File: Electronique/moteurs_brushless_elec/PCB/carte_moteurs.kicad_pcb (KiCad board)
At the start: 2 copper layers, 90 x 65 mm, 82 parts, among them J1 CONN_SERIAL, J2 swdio, J3 FAN, K1 Maxon-200142, K2 Maxon-200142, P1 CONN_I2C, P2 CONN_FREE, P3 CONN_CAN, P4 encoder_2, P5 encoder_1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

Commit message: Noms connecteurs brushless
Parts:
- Encodeur 1: renamed from P5
- Encodeur 2: renamed from P4
- renumbered P3 to CAN, P1 to I2C, P2 to Libre, J1 to Serial
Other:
- board text added: "FAN"
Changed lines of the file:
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@@
   (general
     (links 197)
-    (no_connects 6)
+    (no_connects 0)
     (area 51.6115 80.215 149.459001 152.8396)
     (thickness 1.6)
-    (drawings 14)
+    (drawings 15)
     (tracks 994)
     (zones 0)
@@
   )
   (setup
-    (last_trace_width 0.5)
+    (last_trace_width 1.2)
     (user_trace_width 0.25)
     (user_trace_width 0.5)
@@
     (descr "Connector Headers with Friction Lock, 22-27-2041, http://www.molex.com/pdm_docs/sd/022272021_sd.pdf")
     (tags "connector molex kk_6410 22-27-2041")
-    (fp_text reference P5 (at 1 -4.5) (layer F.SilkS)
+    (fp_text reference "Encodeur 1" (at 3.81 -4.572) (layer F.SilkS)
       (effects (font (size 1 1) (thickness 0.15)))
     )
@@
     (descr "Connector Headers with Friction Lock, 22-27-2021, http://www.molex.com/pdm_docs/sd/022272021_sd.pdf")
     (tags "connector molex kk_6410 22-27-2021")
-    (fp_text reference J1 (at 1 -4.5) (layer F.SilkS)
+    (fp_text reference Serial (at 1 -4.5) (layer F.SilkS)
       (effects (font (size 1 1) (thickness 0.15)))
     )
@@
     (descr "Connector Headers with Friction Lock, 22-27-2021, http://www.molex.com/pdm_docs/sd/022272021_sd.pdf")
     (tags "connector molex kk_6410 22-27-2021")
-    (fp_text reference P1 (at 1 -4.5) (layer F.SilkS)
+    (fp_text reference I2C (at 1.27 -4.572) (layer F.SilkS)
       (effects (font (size 1 1) (thickness 0.15)))
     )
@@
     (descr "Connector Headers with Friction Lock, 22-27-2021, http://www.molex.com/pdm_docs/sd/022272021_sd.pdf")
     (tags "connector molex kk_6410 22-27-2021")
-    (fp_text reference P2 (at 1 -4.5 270) (layer F.SilkS)
+    (fp_text reference Libre (at 1.016 4.826 270) (layer F.SilkS)
       (effects (font (size 1 1) (thickness 0.15)))
     )
@@
     (descr "Connector Headers with Friction Lock, 22-27-2021, http://www.molex.com/pdm_docs/sd/022272021_sd.pdf")
     (tags "connector molex kk_6410 22-27-2021")
-    (fp_text reference P3 (at 1 -4.5) (layer F.SilkS)
+    (fp_text reference CAN (at 1 -4.5) (layer F.SilkS)
       (effects (font (size 1 1) (thickness 0.15)))
     )
@@
     (descr "Connector Headers with Friction Lock, 22-27-2041, http://www.molex.com/pdm_docs/sd/022272021_sd.pdf")
     (tags "connector molex kk_6410 22-27-2041")
-    (fp_text reference P4 (at 1 -4.5 270) (layer F.SilkS)
+    (fp_text reference "Encodeur 2" (at 4.064 4.4704 270) (layer F.SilkS)
       (effects (font (size 1 1) (thickness 0.15)))
     )
@@
     (tags "SOIC 1.27")
     (attr smd)
-    (fp_text reference U9 (at 0 -3.5 180) (layer F.SilkS)
+    (fp_text reference U9 (at 4.826 0.254 180) (layer F.SilkS)
       (effects (font (size 1 1) (thickness 0.15)))
     )
@@
     )
   )
+  (gr_text FAN (at 65.532 146.304 90) (layer F.SilkS)
+    (effects (font (size 1.5 1.5) (thickness 0.3)))
+  )
   (gr_text +3.3V (at 92.8624 91.8464) (layer F.SilkS)

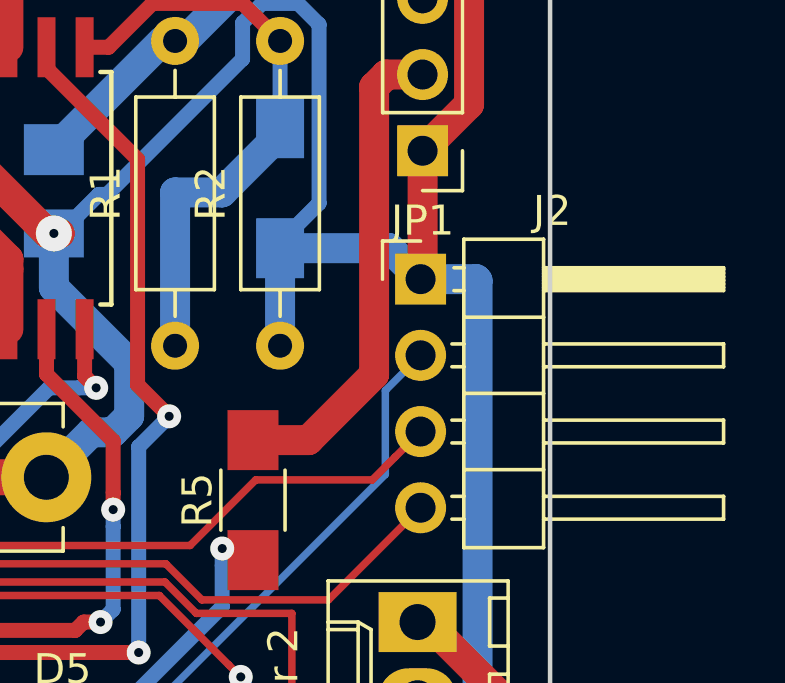
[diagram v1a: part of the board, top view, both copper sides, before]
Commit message: Label st-link brushless
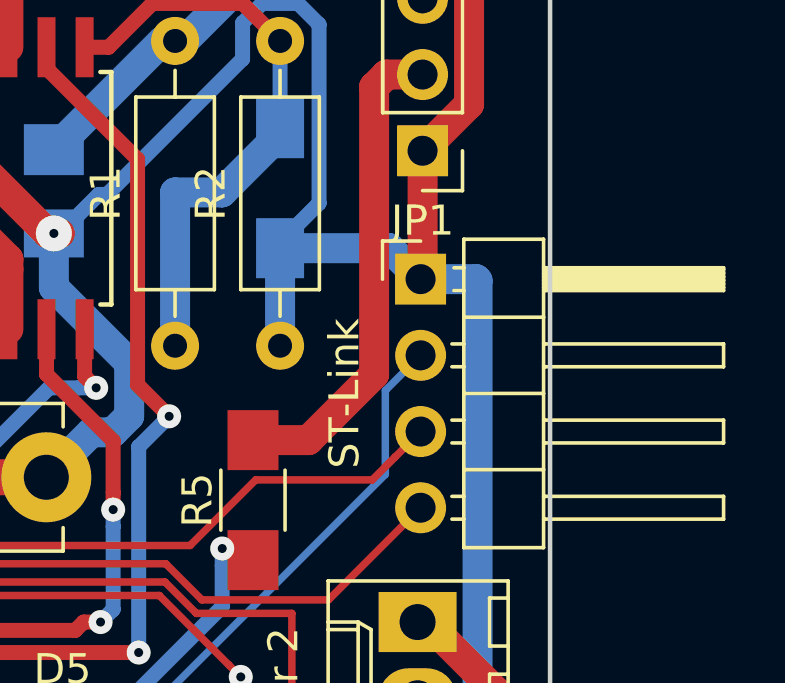
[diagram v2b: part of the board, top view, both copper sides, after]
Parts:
- renumbered J2 to ST-Link
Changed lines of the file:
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@@
     (descr "Through hole angled pin header, 1x04, 2.54mm pitch, 6mm pin length, single row")
     (tags "Through hole angled pin header THT 1x04 2.54mm single row")
-    (fp_text reference J2 (at 4.385 -2.27) (layer F.SilkS)
+    (fp_text reference ST-Link (at -2.54 3.81 90) (layer F.SilkS)
       (effects (font (size 1 1) (thickness 0.15)))
     )
@@
     (connect_pads (clearance 0.508))
     (min_thickness 0.254)
-    (fill (arc_segments 16) (thermal_gap 0.508) (thermal_bridge_width 0.508))
+    (fill yes (arc_segments 16) (thermal_gap 0.508) (thermal_bridge_width 0.508))
     (polygon
       (pts
@@
     (connect_pads (clearance 0.508))
     (min_thickness 0.254)
-    (fill (arc_segments 16) (thermal_gap 0.508) (thermal_bridge_width 0.508))
+    (fill yes (arc_segments 16) (thermal_gap 0.508) (thermal_bridge_width 0.508))
     (polygon
       (pts

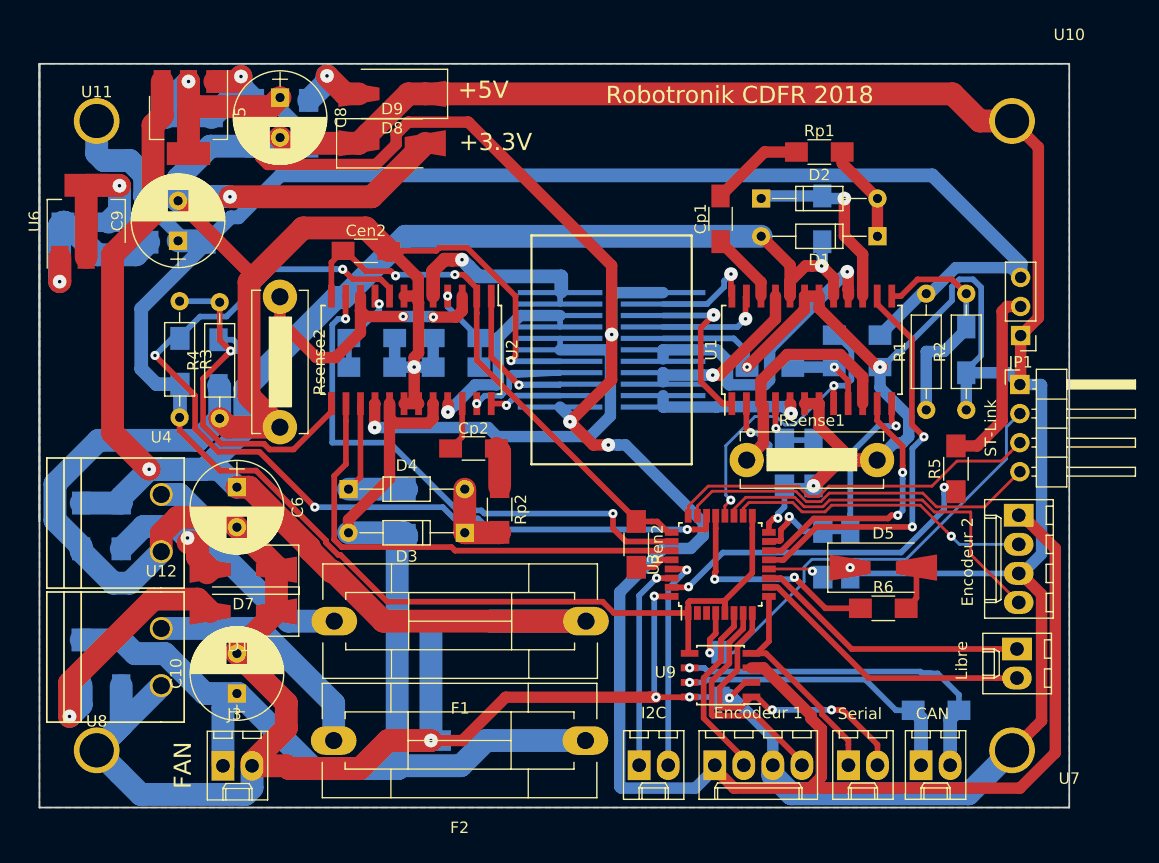
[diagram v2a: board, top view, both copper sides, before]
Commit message: connection 2 pins
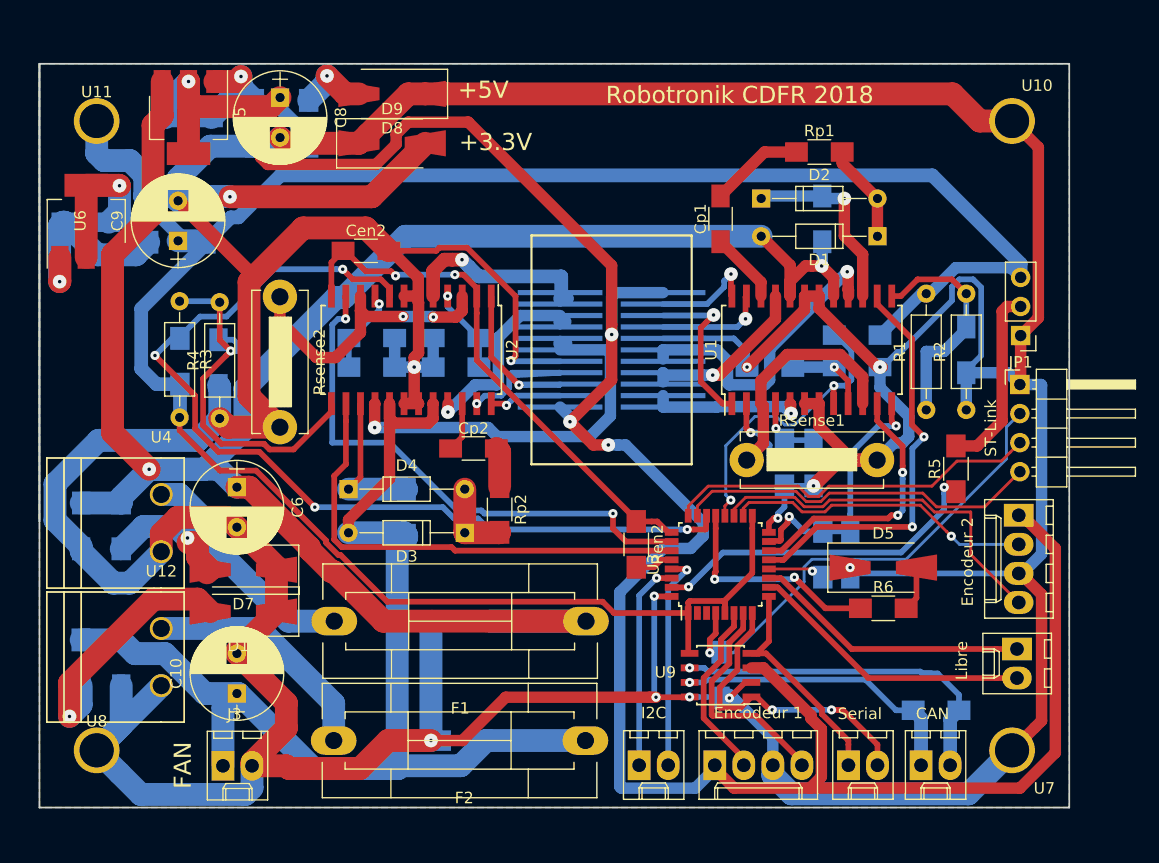
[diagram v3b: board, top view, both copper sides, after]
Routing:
- net Net-(K2-Pad1): track 16.7 -> 17.3 mm
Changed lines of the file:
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@@
-(kicad_pcb (version 4) (host pcbnew 4.0.7)
+(kicad_pcb (version 4) (host pcbnew 4.0.2+dfsg1-stable)
   (general
     (links 197)
     (no_connects 0)
-    (area 51.6115 80.215 149.459001 152.8396)
+    (area 52.924999 80.065 149.459001 151.8298)
     (thickness 1.6)
     (drawings 15)
-    (tracks 994)
+    (tracks 1000)
     (zones 0)
     (modules 82)
@@
     (tags "CMS SOT")
     (attr smd)
-    (fp_text reference U6 (at 0 -4.5 90) (layer F.SilkS)
+    (fp_text reference U6 (at 0.0479 -0.5165 90) (layer F.SilkS)
       (effects (font (size 1 1) (thickness 0.15)))
     )
@@
     (descr "Fuseholder, 5x20, Semi closed, horizontal, Casing 10x25mm,")
     (tags "Fuseholder 5x20 Semi closed horizontal Casing 10x25mm Sicherungshalter halbgeschlossen ")
-    (fp_text reference F2 (at 11 -7.62 180) (layer F.SilkS)
+    (fp_text reference F2 (at 10.5952 -5.0154 180) (layer F.SilkS)
       (effects (font (size 1 1) (thickness 0.15)))
     )
@@
   (module maxon:Trou-3 (layer F.Cu)
     (at 143 150)
-    (fp_text reference U7 (at 0 -2.54) (layer F.SilkS)
+    (fp_text reference U7 (at -2.18 -1.68) (layer F.SilkS)
       (effects (font (size 1 1) (thickness 0.15)))
     )
@@
   (module maxon:Trou-3 (layer F.Cu)
     (at 143 85)
-    (fp_text reference U10 (at 0 -2.54) (layer F.SilkS)
+    (fp_text reference U10 (at -2.82 1.9) (layer F.SilkS)
       (effects (font (size 1 1) (thickness 0.15)))
     )
@@
   (segment (start 113.4364 105.2214) (end 113.515 105.3) (width 0.5) (layer F.Cu) (net 35))
   (via (at 113.4364 103.378) (size 1.2) (drill 0.3) (layers F.Cu B.Cu) (net 35))
-  (segment (start 98.5 105) (end 98.5 106) (width 0.5) (layer B.Cu) (net 36))
+  (segment (start 98.5 105.52) (end 99.11 105.52) (width 1.2) (layer B.Cu) (net 36))
+  (segment (start 98.5 105.52) (end 98.5 106) (width 0.5) (layer B.Cu) (net 36))
+  (segment (start 98.5 105) (end 98.5 105.52) (width 0.5) (layer B.Cu) (net 36))
   (segment (start 87.405 105.3) (end 87.405 103.1) (width 1.2) (layer F.Cu) (net 36))
   (segment (start 87.405 103.1) (end 88.386762 102.118238) (width 1.2) (layer F.Cu) (net 36))
@@
   (via (at 89.9283 102.118238) (size 1.2) (drill 0.3) (layers F.Cu B.Cu) (net 36))
   (segment (start 98.6028 104.8972) (end 98.6028 103.5812) (width 1.2) (layer B.Cu) (net 36))
-  (segment (start 98.5 108) (end 98.5 107) (width 0.5) (layer B.Cu) (net 37))
+  (segment (start 98.5 107.54) (end 98.5 107) (width 0.5) (layer B.Cu) (net 37))
+  (segment (start 98.5 108) (end 98.5 107.54) (width 0.5) (layer B.Cu) (net 37))
+  (segment (start 98.5 107.54) (end 98.9 107.54) (width 1.2) (layer B.Cu) (net 37))
   (segment (start 91.079189 113.056001) (end 89.296799 114.838391) (width 1) (layer B.Cu) (net 37))
   (segment (start 92.968001 113.056001) (end 91.079189 113.056001) (width 1) (layer B.Cu) (net 37))
@@
   (segment (start 88.70501 115.238481) (end 88.6968 115.246691) (width 1) (layer F.Cu) (net 37))
   (via (at 88.6968 115.43839) (size 1.2) (drill 0.3) (layers F.Cu B.Cu) (net 37))
-  (segment (start 98.5 110) (end 98.5 109) (width 0.5) (layer B.Cu) (net 38))
+  (segment (start 98.5 109.45) (end 98.5 109) (width 0.5) (layer B.Cu) (net 38))
+  (segment (start 98.5 110) (end 98.5 109.45) (width 0.5) (layer B.Cu) (net 38))
+  (segment (start 98.5 109.45) (end 98.98 109.45) (width 1.2) (layer B.Cu) (net 38))
   (segment (start 83.144528 116.7892) (end 82.296 116.7892) (width 1) (layer B.Cu) (net 38))
   (segment (start 92.220185 116.7892) (end 83.144528 116.7892) (width 1) (layer B.Cu) (net 38))

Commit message: ecritures
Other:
- board text added: "Vcc"
- board text added: "Vdd"
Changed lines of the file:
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@@
     (area 52.924999 80.065 149.459001 151.8298)
     (thickness 1.6)
-    (drawings 15)
+    (drawings 17)
     (tracks 1000)
     (zones 0)
@@
     )
   )
+  (gr_text Vdd (at 62.29 145.26 90) (layer F.SilkS)
+    (effects (font (size 1.5 1.5) (thickness 0.3)))
+  )
+  (gr_text Vcc (at 55.23 116.1 90) (layer F.SilkS)
+    (effects (font (size 1.5 1.5) (thickness 0.3)))
+  )
   (gr_text FAN (at 65.532 146.304 90) (layer F.SilkS)
